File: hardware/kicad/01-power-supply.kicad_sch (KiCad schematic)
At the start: 36 parts, among them J1 USB_C, J3 JST PH 2-pin, Q1 SI2301CDS, SW16 SS-12D00G3, U2 IP5306, U3 SY8089AAAC, U4 USBLC6-2SC6

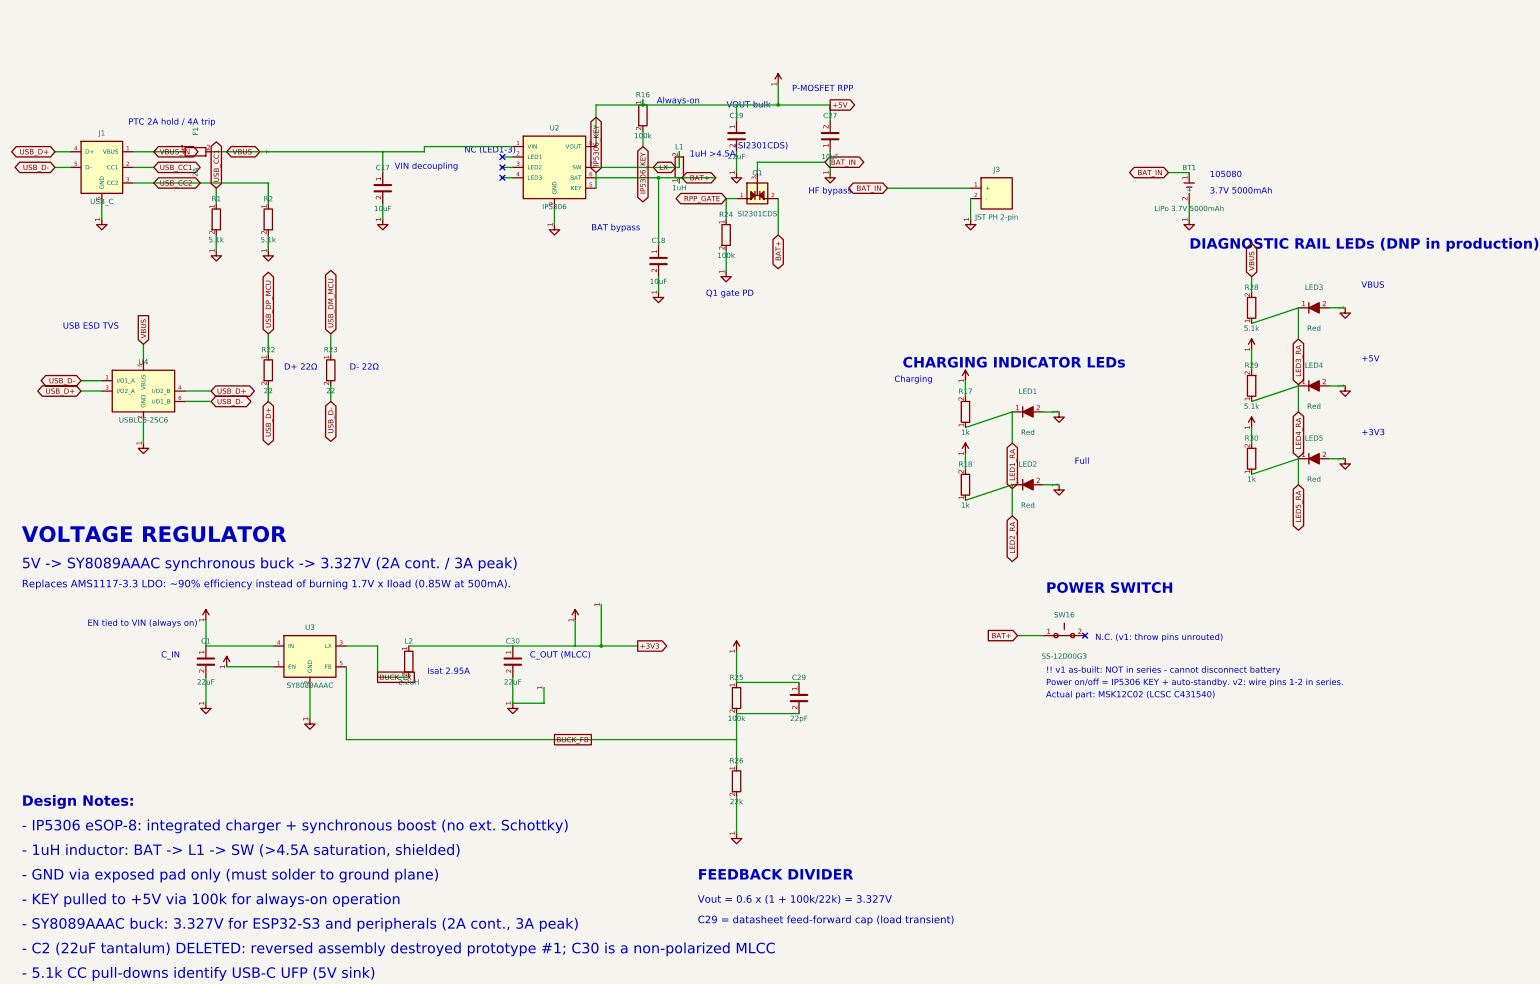
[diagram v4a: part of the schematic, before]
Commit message: schematic: draw the SW16 respin on sheet 01
The sheet still showed the v1 circuit: a switch wired to a BAT+ label and
a no-connect, over the caption "v1 as-built: NOT in series - cannot
disconnect battery". Every schematic-vs-PCB gate was red against it.

The 5 V rail is now drawn as the two nets it is. The VOUT rail keeps
running east from U2.8 but is labelled +5V_VOUT and ends at C27, which is
the only tap left on it — C27 decouples the boost output itself, so it
belongs there. The +5V power symbol that used to sit on that rail is gone:
it would have printed the load rail's name on the boost output, which is
the one thing the split exists to keep apart.

C19 moved with the net. The 22uF bulk hung off the VOUT rail next to C27;
it belongs on the load side, because the inrush it has to supply is what
the loads draw when Q2 turns on. It is drawn next to Q2 now.

R16 is deleted from the sheet. On the load-side +5V that 100k pull-up
would have inverted into a pull-DOWN whenever the switch was OFF and held
KEY asserted. C33 drives KEY instead, and took over R16's footprint site
and its routing on the board.

The POWER SWITCH zone is rebuilt around Q2: SW16 (drawn at 180 deg so its
common — the board's pad 2 — faces the gate network instead of reading
backwards), the PWR_SW spine with R34 and C33 hanging off it, R33 splitting
the gate off, R32 and C32 returning to the SOURCE, and Q2 passing
+5V_VOUT to +5V. The board's pad 3 is deliberately open and so has no pin
on the symbol: with the slider on that side R34 alone defines the node,
which IS the OFF state.

Two things here are easy to draw wrongly and would look right:

  R32 and C32 return to +5V_VOUT, not +5V. Referenced to the load rail
  they would follow the drain down as Q2 turned off and never reach
  V_gs = 0, so the switch could not hold itself off.

  Q2's source is the boost side and its drain is the load side. For a
  P-channel that direction is the entire part: the body diode conducts
  D->S, so this way ro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
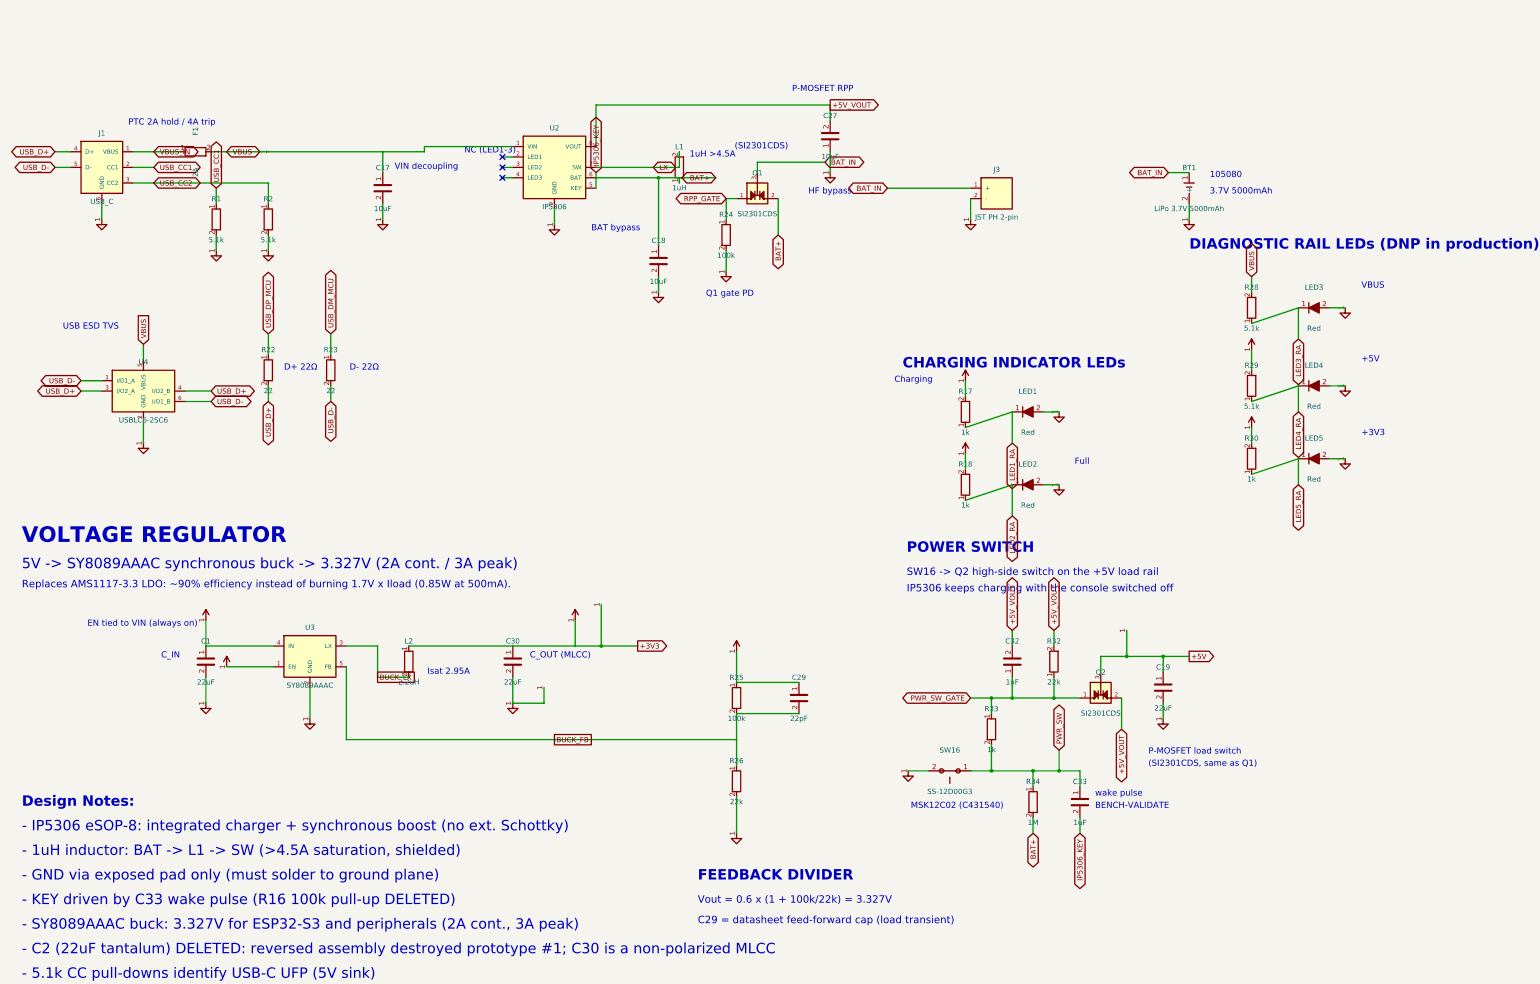
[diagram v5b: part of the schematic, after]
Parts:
- removed C27: 10uF, symbol emu:C
- removed C30: 22uF, symbol emu:C
- removed Q1: SI2301CDS, symbol emu:BAT54C
- removed R16: 100k, symbol emu:R
- added C18: 10uF, symbol emu:C
- added C19: 22uF, symbol emu:C
- added C32: 1uF, symbol emu:C
- added Q2: SI2301CDS, symbol emu:BAT54C
- added R17, R18: 1k, symbol emu:R
- added R34: 1M, symbol emu:R
- added SW16: SS-12D00G3, symbol emu:SW_Push
- added U3: SY8089AAAC, symbol emu:SY8089AAAC
- C27: renamed from C19; value 22uF -> 10uF
- C30: renamed from U3; value SY8089AAAC -> 22uF; symbol emu:SY8089AAAC -> emu:C
- C33: renamed from SW16; value SS-12D00G3 -> 1uF; symbol emu:SW_Push -> emu:C
- Q1: renamed from C18; value 10uF -> SI2301CDS; symbol emu:C -> emu:BAT54C
- R32: renamed from R18; value 1k -> 22k
- renumbered R17 to R33
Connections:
- net +3V3: now also C30.1, R17.2, R18.2; no longer R32.2, R33.2
- net +5V: now also C19.1, Q2.3, U3.1 (EN), U3.4 (IN); no longer C27.1, C30.1 (EN), C30.4 (IN), U2.8 (VOUT)
- net BAT+: now also Q1.2, C18.1, R34.2; no longer C33.1, Q1.1
- net BAT_IN: now also Q1.3
- net BUCK_FB: now also U3.5 (FB); no longer C30.5 (FB)
- net BUCK_LX: now also U3.3 (LX); no longer C30.3 (LX)
- net GND: now also C27.1, C18.2, C19.2, SW16.2, U3.2 (GND); no longer C27.2, Q1.2
- net IP5306_KEY: now also C33.2
- net LED1_RA: now also R17.1; no longer R33.1
- net LED2_RA: now also R18.1; no longer R32.1
- net RPP_GATE: now also Q1.1
- new net +5V_VOUT: C27.2, C32.2, Q2.2, R32.2, U2.8 (VOUT)
- new net PWR_SW: C33.1, R33.2, R34.1, SW16.1
- new net PWR_SW_GATE: C32.1, Q2.1, R32.1, R33.1
- no-connect marks 4 -> 3
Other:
- note added: "(SI2301CDS, same as Q1)"
- note added: "- KEY driven by C33 wake pulse (R16 100k pull-up DELETED)"
- note added: "BENCH-VALIDATE"
- note added: "IP5306 keeps charging with the console switched off"
- note added: "MSK12C02 (C431540)"
- note added: "P-MOSFET load switch"
- note added: "SW16 -> Q2 high-side switch on the +5V load rail"
- note added: "wake pulse"
- note removed: "!! v1 as-built: NOT in series - cannot disconnect battery"
- note removed: "- KEY pulled to +5V via 100k for always-on operation"
- note removed: "Actual part: MSK12C02 (LCSC C431540)"
- note removed: "Always-on"
- note removed: "N.C. (v1: throw pins unrouted)"
- note removed: "Power on/off = IP5306 KEY + auto-standby. v2: wire pins 1-2 in series."
- note removed: "VOUT bulk"
- moved on the sheet: C27, R32, R33

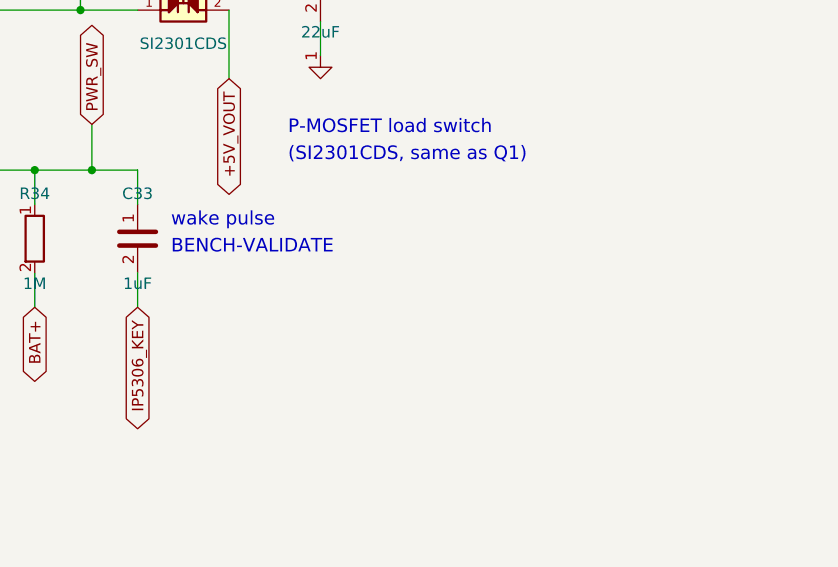
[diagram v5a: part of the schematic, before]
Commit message: SW17: fit the manual KEY wake button, and get every respin barrel off its pad
Two things land together because they are the same reshuffle.

THE VIA-IN-PAD DEFECT. main's new verify_via_in_pad found six barrels
sitting inside SMD lands — R32.2, C32.2, R33.2, R34.1, Q2.2 and Q2.3, all
of them respin copper. It is the JLCDFM "lead to hole distance 0 mm"
DANGER: solder drains down the barrel during reflow and starves the joint.
Q2's two were the deliberate "straddle the seam, one via per pad" design,
so the design was wrong, not just the placement. Every one now steps off
its land with a stub: 0.95 mm west for the 0805s (0.575 pad half-width +
0.15 hole rule + 0.15 barrel radius), and the two Q2 columns start one
step further along instead of at the pad. Both columns keep three barrels,
so the 2.847 A they carry is unchanged.

Retuning those columns surfaced two more, and both were real:
  * the drain column's third barrel landed 75 um from VBUS's F.Cu edge —
    a DANGER in verify_copper_clearance. Shifted 0.15 mm north; 0.225 mm
    now, and the north end still clears Q2.3's pad by 0.175 mm of hole.
  * R34's leg drew a second, overlapping run into the PWR_SW corridor,
    which reads as a 0 degree corner. The corridor was already SPLIT at
    R34's drop precisely so it lands on an endpoint; the split just had to
    follow the via. Both now read one constant, R34_PWR_SW_VIA_X.

SW17. The previous conclusion — no clearance-legal site — was true of the
5.1x5.1 tact the twelve user buttons use, and I can now say so with a
measurement instead of an assertion: scanning x 96..130, y 34..68 on B.Cu
with every respin part AND every piece of respin copper treated as movable
returns sites only north of U2, every one on the far side of the BAT+ B.Cu
run at y=46.1, and the only F.Cu corridor across that run is 0.925 mm wide
(U2's pad edge 113.85 to the gate column's 114.775) and already carries
PWR_SW. A tact there is not a placement problem, it is a re-plan of the
densest corn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
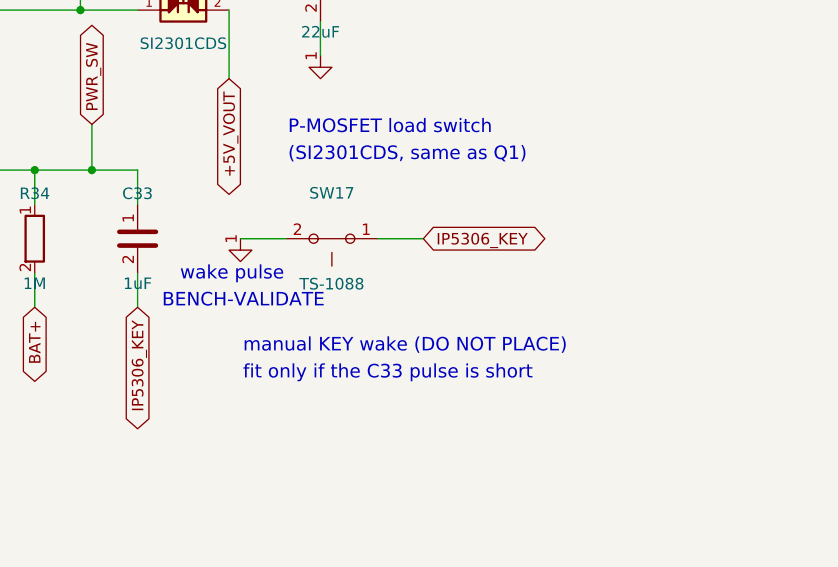
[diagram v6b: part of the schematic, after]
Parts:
- removed C19: 22uF, symbol emu:C
- added C32: 1uF, symbol emu:C
- added R17: 1k, symbol emu:R
- C19: renamed from R17; value 1k -> 22uF; symbol emu:R -> emu:C
- R33: renamed from C32; value 1uF -> 1k; symbol emu:C -> emu:R
- SW17: renamed from R33; value 1k -> TS-1088; symbol emu:R -> emu:SW_Push
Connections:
- net +3V3: now also R17.2; no longer C19.2
- net +5V: now also C19.1
- net +5V_VOUT: now also C32.2; no longer R33.2
- net GND: now also C19.2, SW17.2
- net IP5306_KEY: now also SW17.1
- net LED1_RA: now also R17.1; no longer C19.1
- net PWR_SW: now also R33.2; no longer SW17.2
- net PWR_SW_GATE: now also C32.1; no longer SW17.1
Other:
- note added: "fit only if the C33 pulse is short"
- note added: "manual KEY wake (DO NOT PLACE)"
